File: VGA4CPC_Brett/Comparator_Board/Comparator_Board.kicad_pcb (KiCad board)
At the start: 2 copper layers, 35 x 20 mm, 18 parts, among them J1 INPUT, J2 OUTPUT, U1 TLV3232, U2 TLV3232, U3 TLV3232

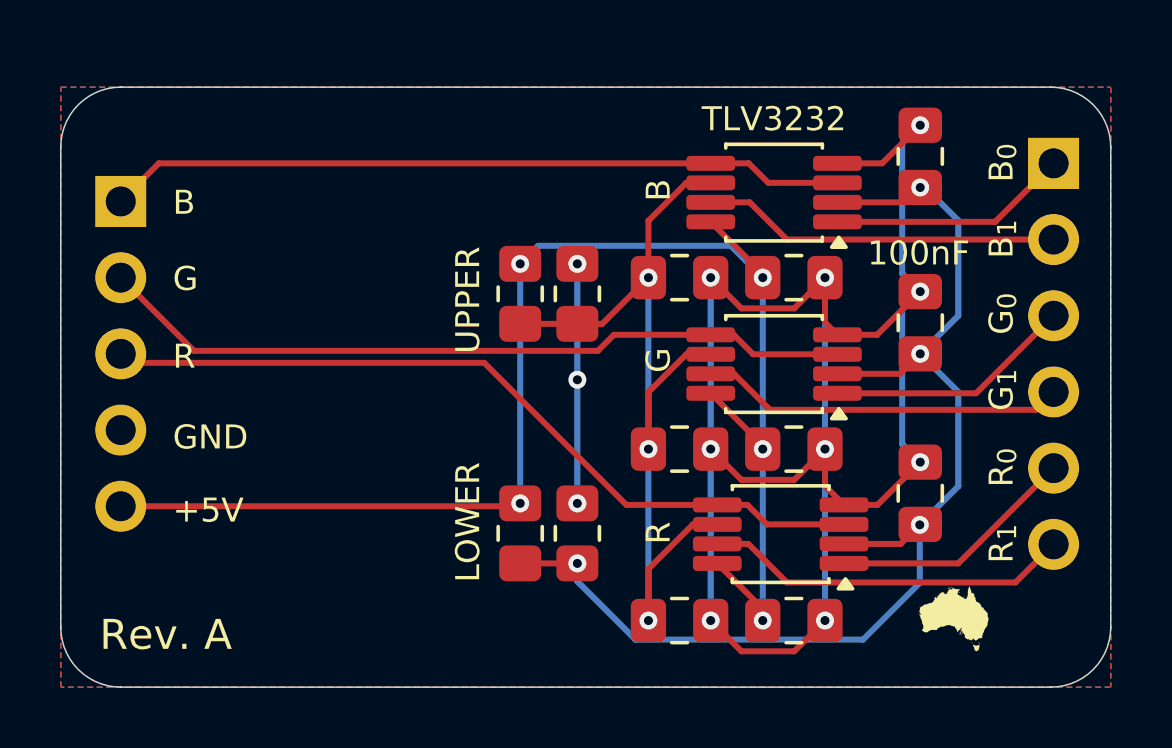
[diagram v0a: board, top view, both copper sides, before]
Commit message: Finalised voltage divider resistor values
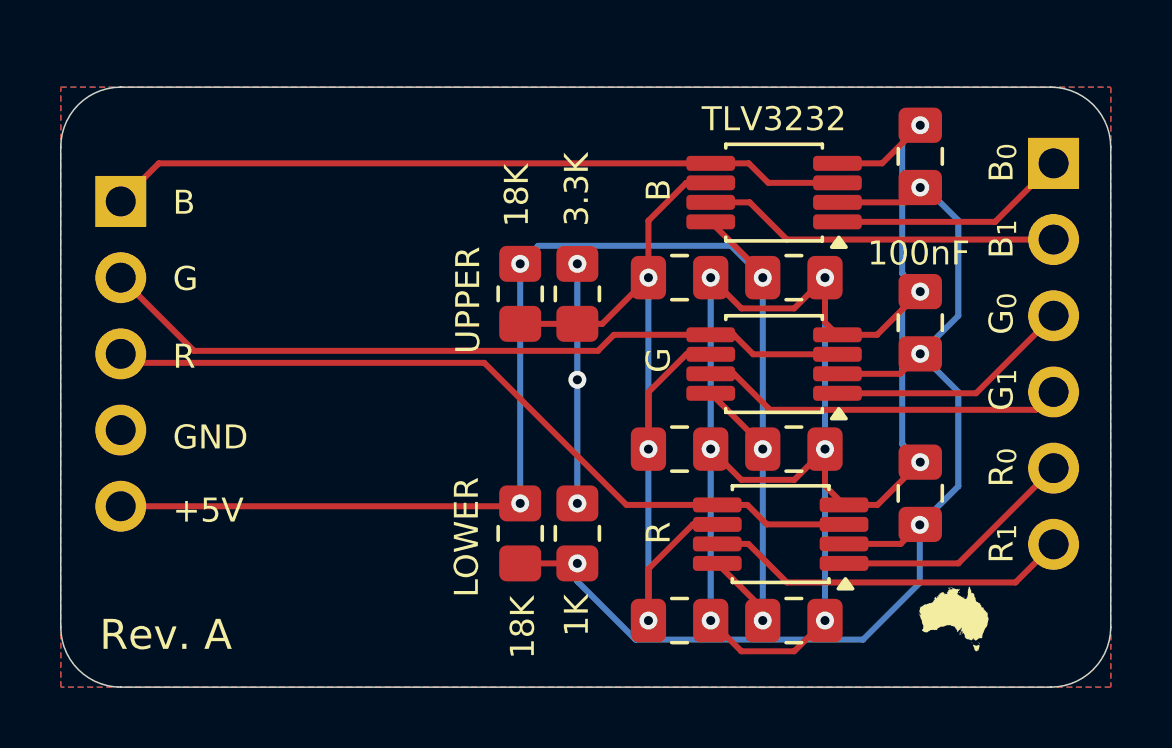
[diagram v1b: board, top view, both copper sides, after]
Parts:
- R1: value 17KΩ -> 18K
- R2: value 3KΩ -> 3.3K
- R3: value 19KΩ -> 18K
- R4: value 1KΩ -> 1K
